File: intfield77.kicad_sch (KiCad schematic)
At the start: 0 parts

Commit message: Started on MCU and USB-C connector.
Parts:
- added C1, C4: 4.7u, symbol Device:C_Small
- added C2, C3, C5: 0.1u, symbol Device:C_Small
- added C6, C8, C9: 1.0u, symbol Device:C_Small
- added C7: 0.01u, symbol Device:C_Small
- added F1: 500mA, symbol Device:Polyfuse_Small
- added J1: USB_C_Receptacle_USB2.0, symbol Connector:USB_C_Receptacle_USB2.0
- added R1, R2: 5.1k, symbol Device:R_Small
- added U1: STM32F072C8Tx, Package_QFP:LQFP-48_7x7mm_P0.5mm, symbol MCU_ST_STM32F0:STM32F072C8Tx
- added U2: SRV05-4, Package_TO_SOT_SMD:SOT-23-6, symbol Power_Protection:SRV05-4
- added U3: TC1262-33, symbol Regulator_Linear:TC1262-33
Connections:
- new net: J1.B5 (CC2), R1.1
- new net: J1.A5 (CC1), R2.1
- new net +3.3V: C1.1, C2.1, C3.1, C4.1, C5.1, C6.1, C7.1, C9.1, U1.24 (VDD), U1.36 (VDDIO2), U1.48 (VDD), U1.9 (VDDA), U3.3 (VO)
- new net +5V: C8.1, F1.2, U3.1 (VI)
- new net BOOT: U1.44 (BOOT0)
- new net D+: J1.A6 (D+), J1.B6 (D+), U1.33 (PA12), U2.3 (IO2)
- new net D-: J1.A7 (D-), J1.B7 (D-), U1.32 (PA11), U2.4 (IO3)
- new net GND: C1.2, C2.2, C3.2, C4.2, C5.2, C6.2, C7.2, C8.2, C9.2, J1.A1 (GND), J1.A12 (GND), J1.B1 (GND), J1.B12 (GND), R1.2, R2.2, U1.23 (VSS), U1.35 (VSS), U1.47 (VSS), U1.8 (VSSA), U2.2 (VN), U3.2 (GND)
- new net NRST: U1.7 (NRST)
- new net VBUS: F1.1, J1.A4 (VBUS), J1.A9 (VBUS), J1.B4 (VBUS), J1.B9 (VBUS), U2.5 (VP)
- new net XTAL_IN: U1.5 (PF0)
- new net XTAL_OUT: U1.6 (PF1)
- no-connect marks 0 -> 5
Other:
- added sheet Matrix (matrix.kicad_sch)

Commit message: First version of schematic, including duplex matrix.
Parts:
- removed U3: TC1262-33, symbol Regulator_Linear:TC1262-33
- added C10: 0.1u, symbol Device:C_Small
- added J2: TC2030, Connector:Tag-Connect_TC2030-IDC-FP_2x03_P1.27mm_Vertical, symbol Connector:Conn_ARM_SWD_TagConnect_TC2030
- added R3: 10k, symbol Device:R_Small
- added SW1: RESET, symbol Switch:SW_Push
- added SW2: BOOT, symbol Switch:SW_DIP_x01
- added U3: XC6206PxxxMR, Package_TO_SOT_SMD:SOT-23-3, symbol Regulator_Linear:XC6206PxxxMR
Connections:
- net +3.3V: now also J2.1 (VCC), SW2.1, U3.2 (VO)
- net +5V: now also U3.3 (VI)
- net BOOT: now also R3.1, SW2.2
- net GND: now also J1.S1 (SHIELD), C10.2, J2.5 (GND), R3.2, SW1.1, U3.1 (GND)
- net NRST: now also C10.1, J2.3 (~{RESET}), SW1.2
- net NUM: now reaches U1.10 (PA0)
- net NUM: now also U1.39 (PB3), U1.40 (PB4), U1.41 (PB5), U1.42 (PB6), U1.43 (PB7), U1.45 (PB8), U1.46 (PB9)
- net KEY: now reaches U1.11 (PA1)
- net KEY: now also U1.12 (PA2), U1.13 (PA3), U1.14 (PA4), U1.15 (PA5), U1.16 (PA6), U1.17 (PA7), U1.18 (PB0), U1.19 (PB1), U1.20 (PB2), U1.21 (PB10), U1.22 (PB11), U1.25 (PB12), U1.26 (PB13), U1.27 (PB14), U1.28 (PB15)
- net SWDIO: now reaches U1.34 (PA13)
- net SWDIO: now also J2.2 (SWDIO)
- net SWCLK: now reaches U1.37 (PA14)
- net SWCLK: now also J2.4 (SWCLK)
- net XTAL_IN: no longer names the net of U1.5 (PF0)
- net XTAL_OUT: no longer names the net of U1.6 (PF1)
- no-connect marks 5 -> 15

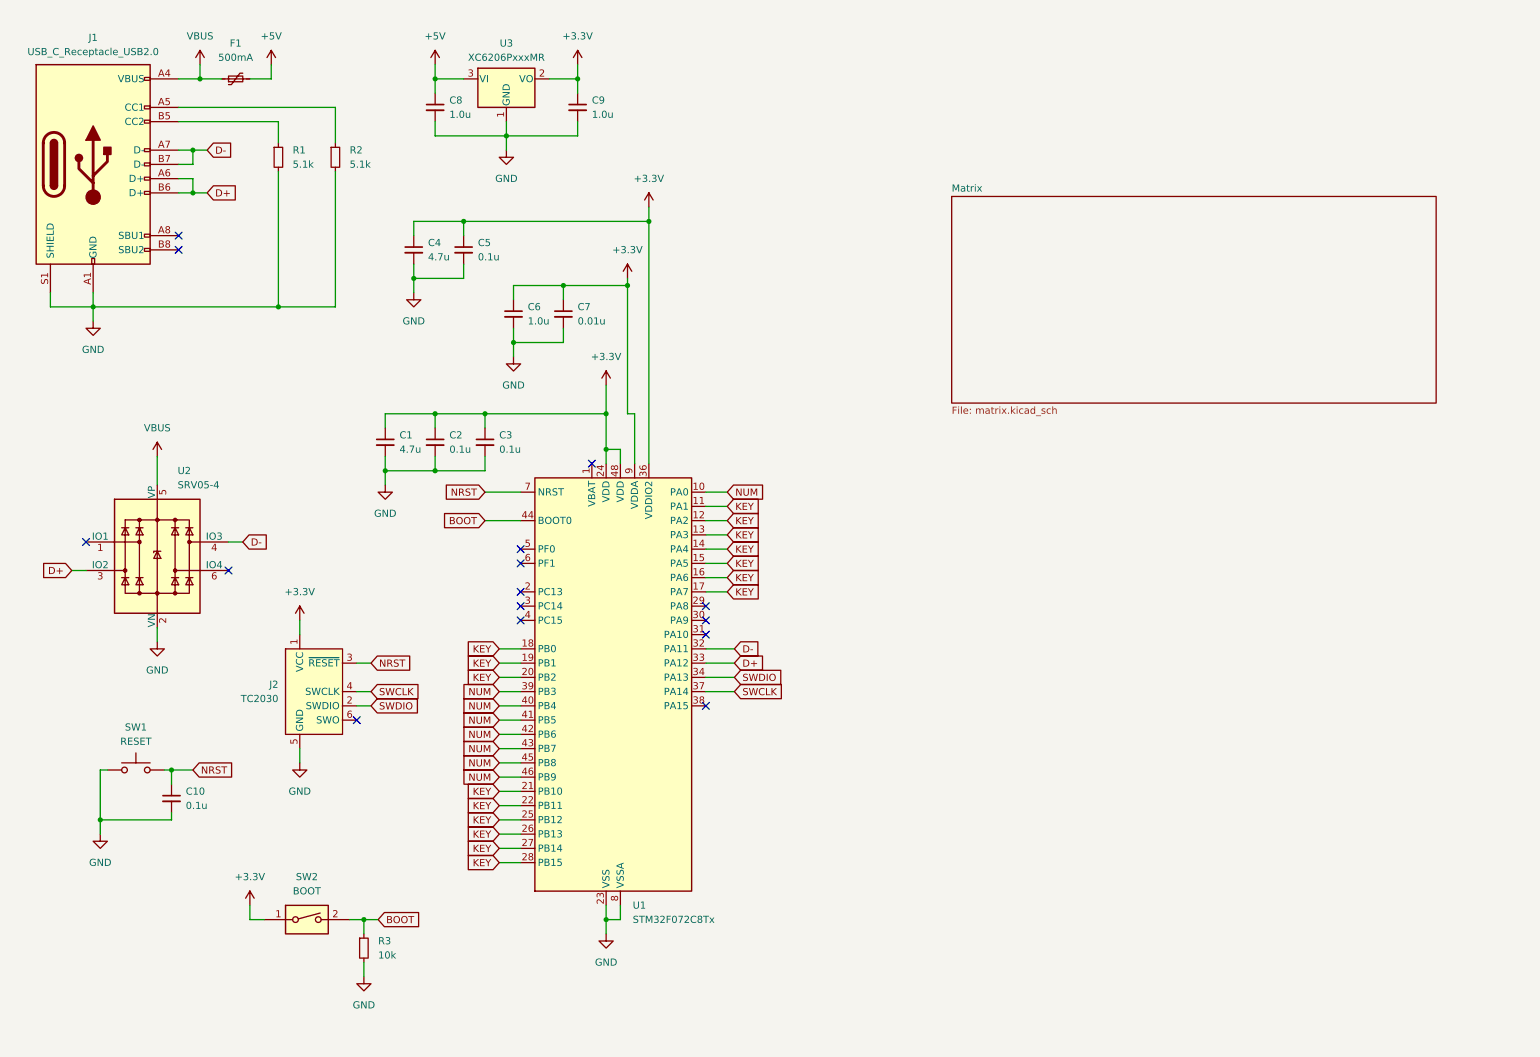
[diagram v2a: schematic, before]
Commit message: Trying to connect the matrix sheet with the main sheet.
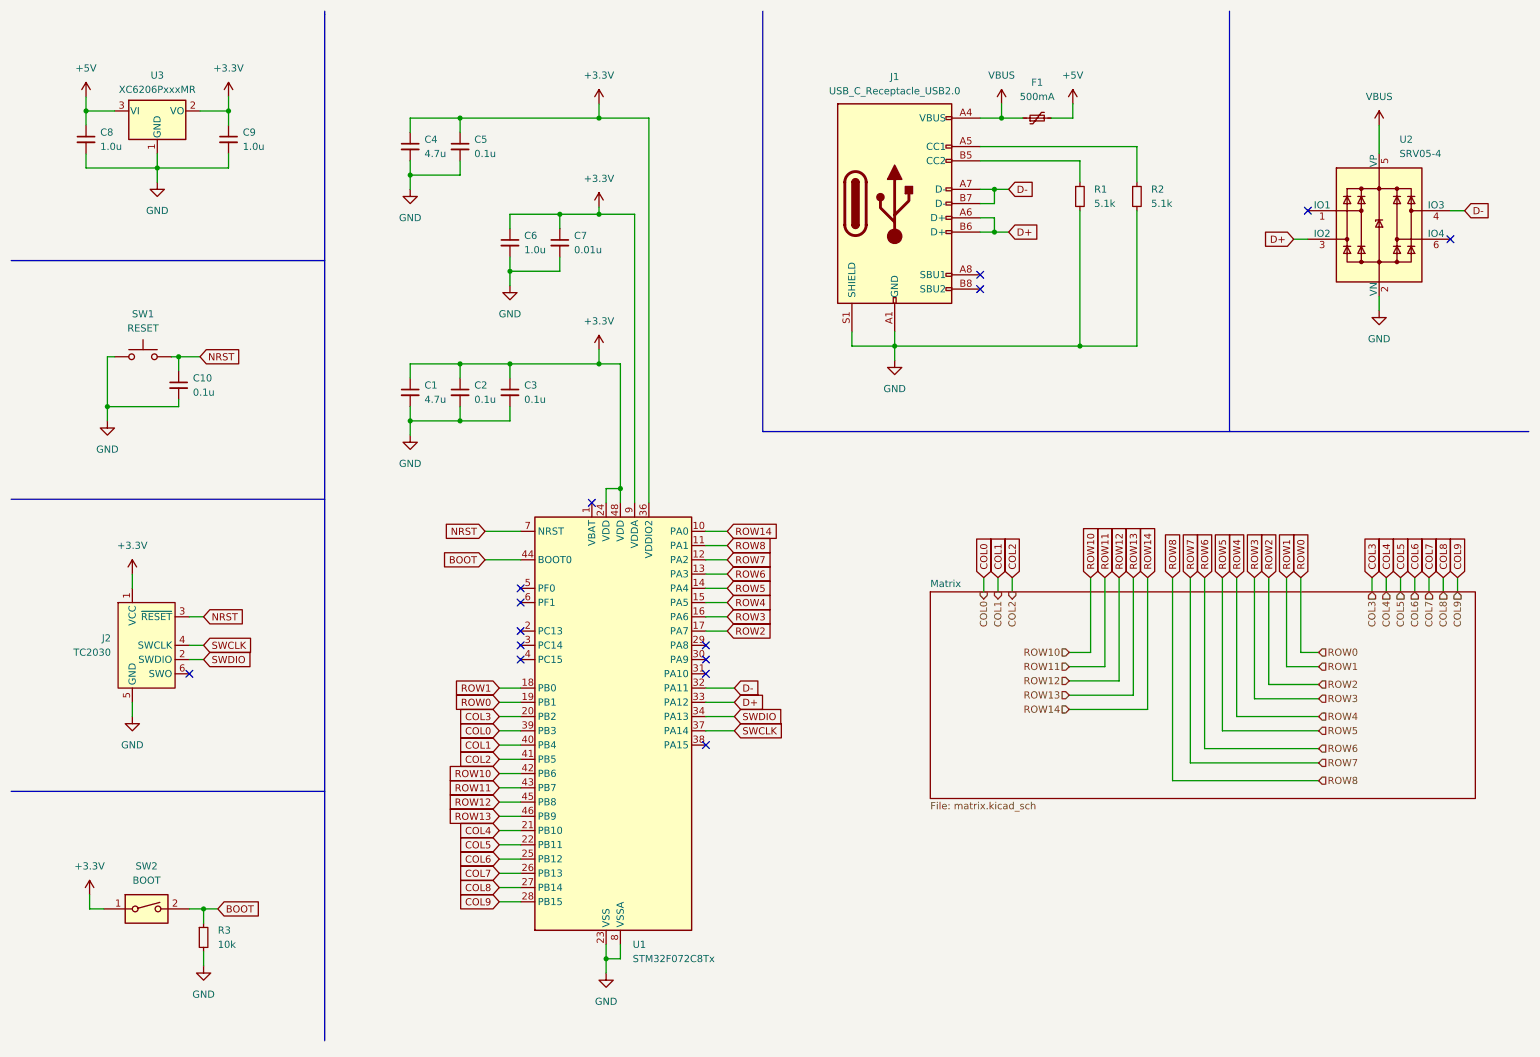
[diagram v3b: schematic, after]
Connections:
- removed net KEY: U1.11 (PA1), U1.12 (PA2), U1.13 (PA3), U1.14 (PA4), U1.15 (PA5), U1.16 (PA6), U1.17 (PA7), U1.18 (PB0), U1.19 (PB1), U1.20 (PB2), U1.21 (PB10), U1.22 (PB11), U1.25 (PB12), U1.26 (PB13), U1.27 (PB14), U1.28 (PB15)
- removed net NUM: U1.10 (PA0), U1.39 (PB3), U1.40 (PB4), U1.41 (PB5), U1.42 (PB6), U1.43 (PB7), U1.45 (PB8), U1.46 (PB9)
- new net COL0: U1.39 (PB3)
- new net COL1: U1.40 (PB4)
- new net COL2: U1.41 (PB5)
- new net COL3: U1.20 (PB2)
- new net COL4: U1.21 (PB10)
- new net COL5: U1.22 (PB11)
- new net COL6: U1.25 (PB12)
- new net COL7: U1.26 (PB13)
- new net COL8: U1.27 (PB14)
- new net COL9: U1.28 (PB15)
- new net ROW0: U1.19 (PB1)
- new net ROW1: U1.18 (PB0)
- new net ROW10: U1.42 (PB6)
- new net ROW11: U1.43 (PB7)
- new net ROW12: U1.45 (PB8)
- new net ROW13: U1.46 (PB9)
- new net ROW14: U1.10 (PA0)
- new net ROW2: U1.17 (PA7)
- new net ROW3: U1.16 (PA6)
- new net ROW4: U1.15 (PA5)
- new net ROW5: U1.14 (PA4)
- new net ROW6: U1.13 (PA3)
- new net ROW7: U1.12 (PA2)
- new net ROW8: U1.11 (PA1)
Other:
- moved on the sheet: C1, C10, C2, C3, C4, C5, C6, C7, C8, C9, F1, J1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

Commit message: Matrix is connected to rest of schematic.
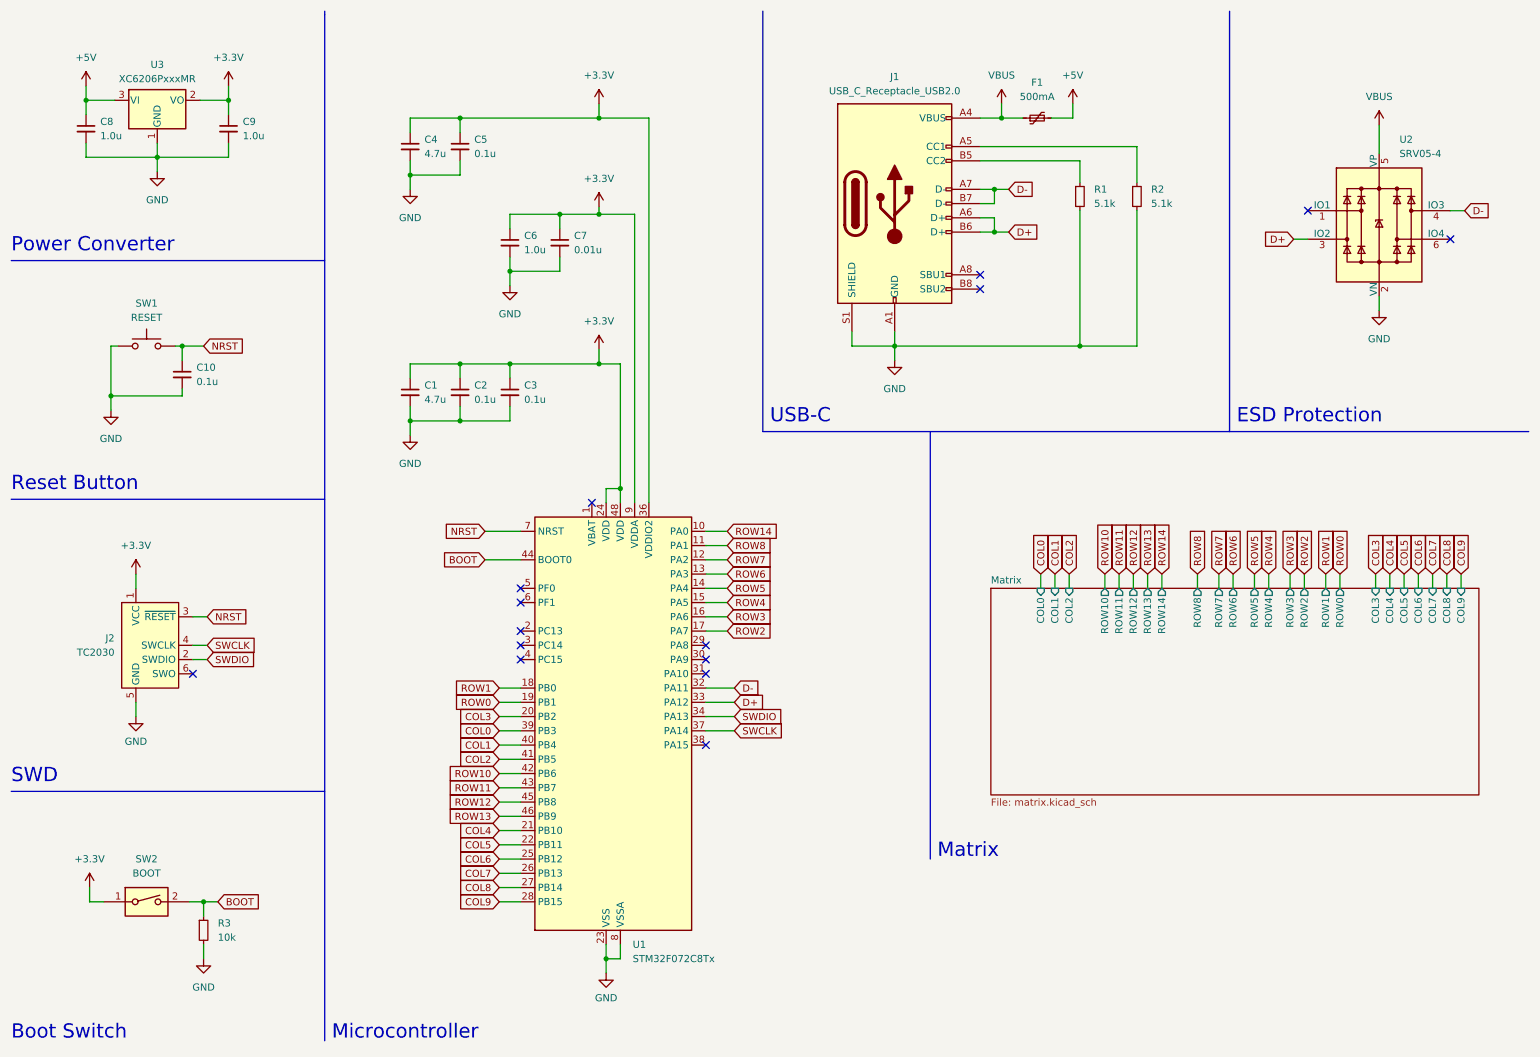
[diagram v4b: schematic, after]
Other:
- sheet Matrix ports: added COL0, COL1, COL2, COL3, COL4, COL5, COL6, COL7, COL8, COL9, ROW0, ROW1, ROW10, ROW11, ROW12, ROW13, ROW14, ROW2, ROW3, ROW4, ROW5, ROW6, ROW7, ROW8; removed none
- note added: "Boot Switch"
- note added: "ESD Protection"
- note added: "Matrix"
- note added: "Microcontroller"
- note added: "Power Converter"
- note added: "Reset Button"
- note added: "SWD"
- note added: "USB-C"
- moved on the sheet: C10, C8, C9, J2, R3, SW1, SW2, U3

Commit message: Assigned footprints, key labels and placed key switches on PCB. Removed SWD component.
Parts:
- removed J2: TC2030, Connector:Tag-Connect_TC2030-IDC-FP_2x03_P1.27mm_Vertical, symbol Connector:Conn_ARM_SWD_TagConnect_TC2030
- C1, C10, C2, C3, C4, C5, C6, C7, C8, C9: footprint (none) -> Capacitor_SMD:C_0805_2012Metric
- F1: footprint (none) -> Fuse:Fuse_1206_3216Metric
- J1: footprint (none) -> Type-C:HRO-TYPE-C-31-M-12-Assembly
- R1, R2, R3: footprint (none) -> Resistor_SMD:R_0815_2038Metric
- SW1: footprint (none) -> random-keyboard-parts:SKQGADE010
- SW2: footprint (none) -> Button_Switch_SMD:SW_DIP_SPSTx01_Slide_9.78x4.72mm_W8.61mm_P2.54mm
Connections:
- no-connect marks 15 -> 16
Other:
- title: (none) -> Intfield77
- moved on the sheet: F1, J1, R1, R2
